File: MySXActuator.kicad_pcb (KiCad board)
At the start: 2 copper layers, 27.7 x 38.1 mm, 30 parts, among them Q1 2N7002, Q2 IRF540N, Q3 IRF540N, Q4 2N7002, U1 AP63205WU

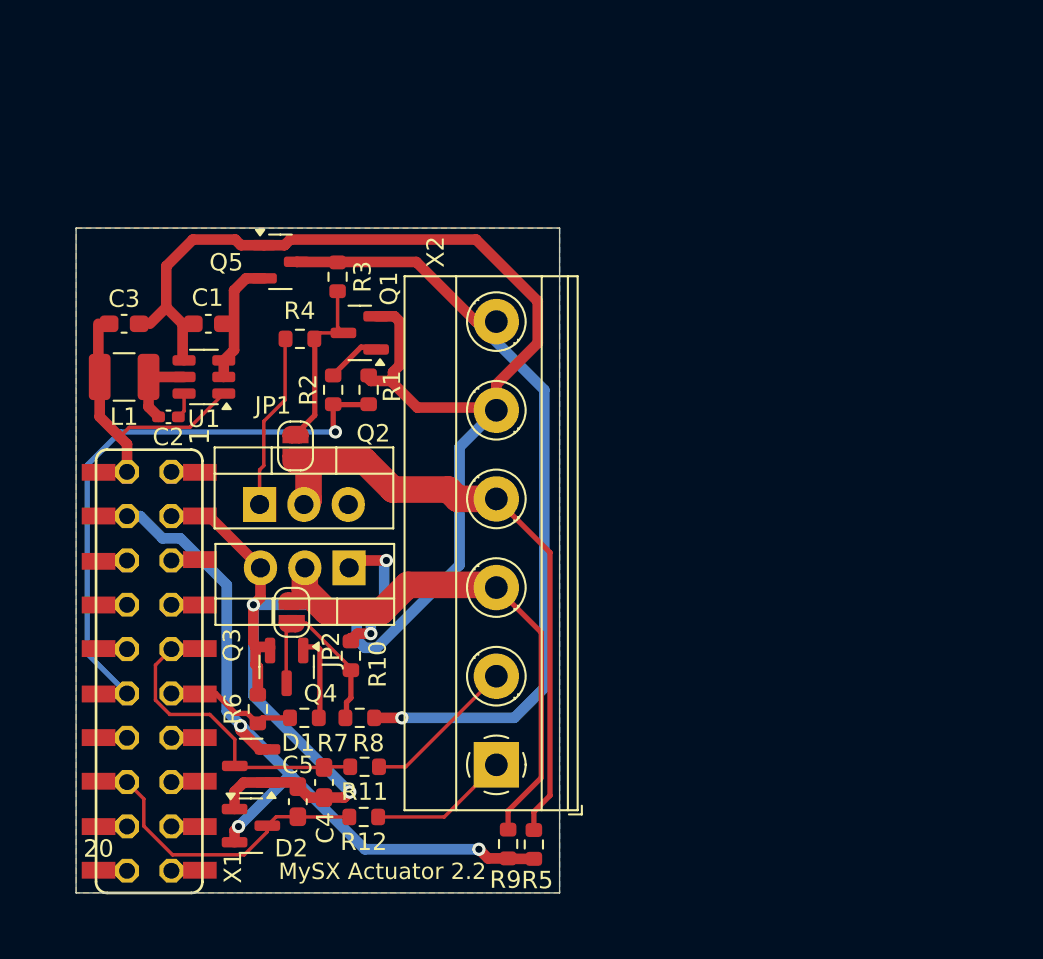
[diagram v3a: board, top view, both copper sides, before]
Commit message: update schematic
- add zener diode to protect high positive voltage on inputs
- add anoter 2 input sections as alternative to led drivers
- add add rj45 socket for i2c interface
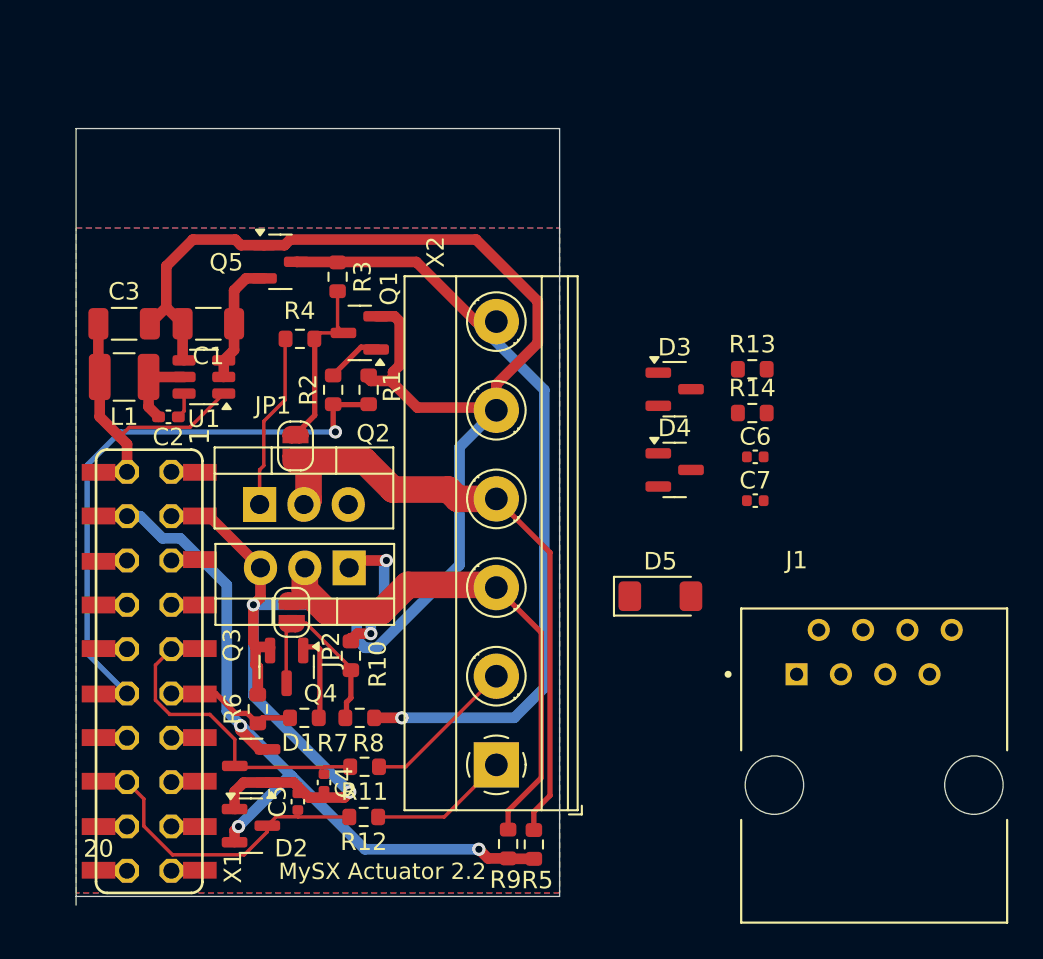
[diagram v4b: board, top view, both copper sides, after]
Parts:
- added C6: 10n/50V, Capacitor_SMD:C_0402_1005Metric, F.Cu at (174.2, 99.1)
- added C7: 10n/50V, Capacitor_SMD:C_0402_1005Metric, F.Cu at (174.2, 101.6)
- added D3: BAT54S, Package_TO_SOT_SMD:SOT-23, F.Cu at (169.6, 95.2)
- added D4: BAT54S, Package_TO_SOT_SMD:SOT-23, F.Cu at (169.6, 99.8)
- added D5: 3.6V, Diode_SMD:D_MiniMELF, F.Cu at (168.8, 107.0)
- added J1: 8P8C, MySXActuator:AMPHENOL_54601-908WPLF, F.Cu at (181.0, 117.9)
- added R13: 2k, Resistor_SMD:R_0603_1608Metric, F.Cu at (174.0, 94.0)
- added R14: 2k, Resistor_SMD:R_0603_1608Metric, F.Cu at (174.0, 96.6)
- C1, C3: footprint Capacitor_SMD:C_0603_1608Metric_Pad1.08x0.95mm_HandSolder -> Capacitor_SMD:C_1206_3216Metric
- C4, C5: value 10n -> 10n/50V; footprint Capacitor_SMD:C_0603_1608Metric_Pad1.08x0.95mm_HandSolder -> Capacitor_SMD:C_0402_1005Metric
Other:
- board size 27.7 x 38.1 mm -> 27.7 x 44.5 mm

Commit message: update PCB after schematic changes
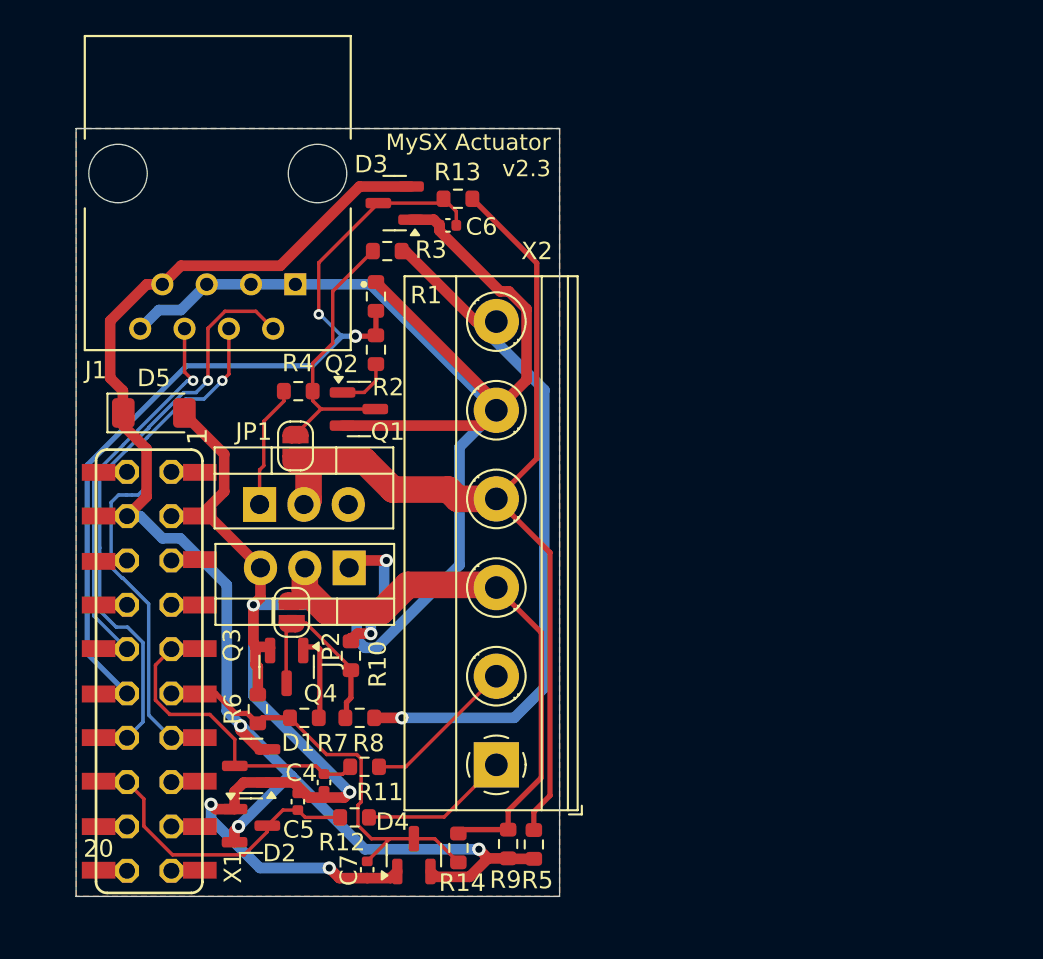
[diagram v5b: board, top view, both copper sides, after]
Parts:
- removed C1: 10u/50V, Capacitor_SMD:C_1206_3216Metric
- removed C2: 100n/50V, Capacitor_SMD:C_0402_1005Metric_Pad0.74x0.62mm_HandSolder
- removed C3: 10u, Capacitor_SMD:C_1206_3216Metric
- removed L1: 4.7u, Inductor_SMD:L_1210_3225Metric
- removed Q5: ~, Package_TO_SOT_SMD:SOT-23
- removed U1: AP63205WU, Package_TO_SOT_SMD:TSOT-23-6
- moved J1 51.4 mm to (143.4, 82.8), turned to 180 degrees
- moved D5 30.9 mm to (139.8, 96.5)
- moved C7 30.7 mm to (152.0, 122.7), turned to -90 degrees
- moved R14 30.1 mm to (157.2, 121.5), turned to -90 degrees
- moved D4 26.7 mm to (154.7, 121.9), turned to 90 degrees
- moved C6 22.0 mm to (156.6, 85.8), turned to 180 degrees
- moved R13 19.5 mm to (157.2, 84.3), turned to 180 degrees
- moved D3 19.3 mm to (153.6, 84.5), turned to 180 degrees
- moved R1 5.37 mm to (152.5, 89.9)
- moved Q1 4.36 mm to (151.5, 96.3), turned to 0 degrees
- moved R2 3.36 mm to (152.5, 92.9), turned to -90 degrees
- moved R3 3.20 mm to (153.1, 87.3), turned to 180 degrees
- moved R4 3.00 mm to (148.0, 95.3)
- moved R12 0.53 mm to (151.2, 119.7)
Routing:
- net VCCIO: track 43.2 -> 80.0 mm
- net D7_SCL: track 0.00 -> 32.8 mm, vias 0 -> 1
- net GND: track 113.2 -> 143.0 mm, vias 2 -> 4
- net D8_SDA: track 0.00 -> 29.0 mm, vias 0 -> 1
- net D3_INT: track 0.00 -> 22.1 mm, vias 0 -> 1
- net LED1: track 35.7 -> 55.4 mm
- net D5_PWM: track 32.7 -> 50.4 mm, vias 1 -> 2
- net D6_PWM: track 7.68 -> 25.1 mm
- net VRAW: track 16.2 -> 0.00 mm
- net Net-(Q5-S): track 7.21 -> 0.00 mm
- net VIN: track 46.1 -> 40.4 mm
- net Net-(JP1-A): track 10.3 -> 15.9 mm
- net Net-(U1-SW): track 4.56 -> 0.00 mm
- net Net-(Q2-G): track 10.1 -> 7.12 mm
- net LED2: track 31.0 -> 33.9 mm
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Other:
- board size 27.7 x 44.5 mm -> 27.7 x 44 mm
- board text added: "MySX Actuator v2.3"
- board text removed: "MySX Actuator 2.2"

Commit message: Add removed buck converter
- previously removed buck converter is needed to not require power from
RS485 line
- position RJ45 connector closer to center of the board to allow use
straigth connector (facing up)
- replace THT power transistors with SMT power transistors
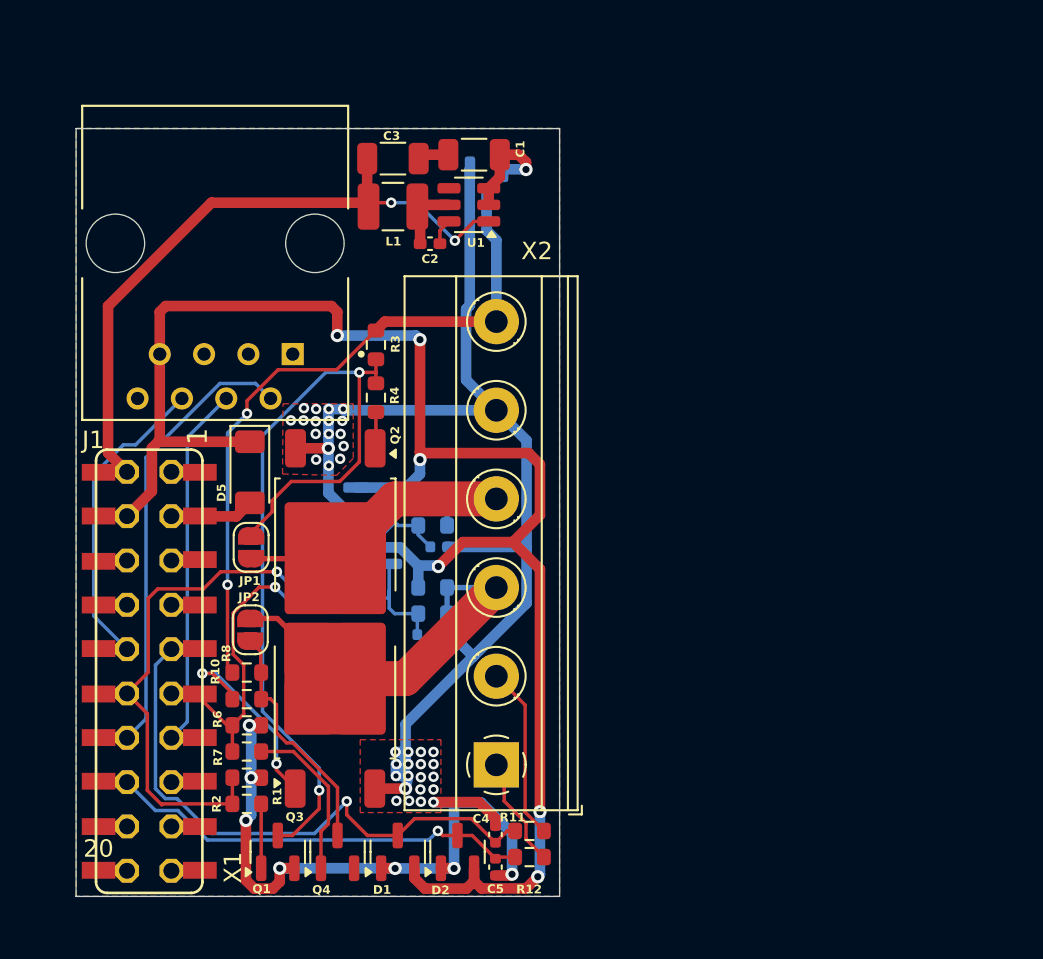
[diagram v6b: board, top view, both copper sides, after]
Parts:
- added C1: 10u/50V, Capacitor_SMD:C_1206_3216Metric, F.Cu at (158.1, 81.8)
- added C2: 100n/50V, Capacitor_SMD:C_0402_1005Metric_Pad0.74x0.62mm_HandSolder, F.Cu at (155.6, 86.8)
- added C3: 10u, Capacitor_SMD:C_1206_3216Metric, F.Cu at (153.4, 82.0)
- added L1: 4.7u, Inductor_SMD:L_1210_3225Metric, F.Cu at (153.4, 84.7)
- added Q5: ~, Package_TO_SOT_SMD:SOT-23, B.Cu at (158.8, 83.5)
- added U1: AP63205WU, Package_TO_SOT_SMD:TSOT-23-6, F.Cu at (157.8, 84.6)
- C6, C7, D3, D4, R13, R14, R5, R9: moved to B.Cu
- Q2, Q3: value IRF540N -> IRFR7546PbF; footprint Package_TO_SOT_THT:TO-220-3_Vertical -> Package_TO_SOT_SMD:TO-252-2
- moved R1 28.6 mm to (145.1, 117.5), turned to 0 degrees
- moved R2 27.1 mm to (145.1, 119.0), turned to 0 degrees
- moved Q1 25.8 mm to (146.8, 121.7), turned to 90 degrees
- moved R5 20.6 mm to (155.7, 101.5), turned to 0 degrees
- moved R13 18.8 mm to (155.7, 103.0)
- moved C6 18.4 mm to (156.1, 104.2), turned to 0 degrees
- moved D3 17.3 mm to (152.3, 101.8), turned to 0 degrees
- moved D4 16.9 mm to (152.3, 105.2), turned to 0 degrees
- moved R9 15.3 mm to (155.7, 106.5), turned to 0 degrees
- moved C7 13.9 mm to (155.3, 109.2), turned to 0 degrees
- moved R14 13.5 mm to (155.7, 108.0), turned to 180 degrees
- moved D2 11.9 mm to (157.2, 121.7), turned to 90 degrees
- moved C5 11.9 mm to (159.3, 122.6), turned to -90 degrees
- moved Q4 11.0 mm to (150.3, 121.7), turned to 90 degrees
- moved R12 10.3 mm to (161.3, 122.0)
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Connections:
- net D3_RX renamed D2_RX
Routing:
- net VRAW: track 0.00 -> 38.3 mm, vias 0 -> 2
- net LED1: track 55.4 -> 19.8 mm
- net Net-(JP1-A): track 15.9 -> 48.7 mm, vias 0 -> 2
- net VCCIO: track 80.0 -> 99.7 mm, vias 3 -> 6
- net GND: track 143.0 -> 126.0 mm, vias 4 -> 43
- net D4_INT: track 17.3 -> 33.3 mm, vias 0 -> 1
- net LED2: track 33.9 -> 19.8 mm
- net D8_SDA: track 29.0 -> 20.7 mm, vias 1 -> 0
- net D9_A3: track 16.3 -> 24.5 mm, vias 0 -> 1
- net D7_SCL: track 32.8 -> 25.8 mm, vias 1 -> 0
- net +24V: track 0.00 -> 6.56 mm, vias 0 -> 1
- net Net-(Q2-G): track 7.12 -> 2.09 mm
- net D5_PWM: track 50.4 -> 45.4 mm, vias 2 -> 1
- net Net-(Q4-G): track 4.97 -> 9.54 mm
- net D3_INT: track 22.1 -> 17.7 mm, vias 1 -> 0
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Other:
- board text added: "GND"
- board text added: "LED1"
- board text added: "LED2"
- board text added: "MySX Actuator v2.4"
- board text added: "SW1"
- board text added: "SW2"
- board text added: "VIN"
- board text removed: "MySX Actuator v2.3"

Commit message: update to new kicad version 8.0
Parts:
- Q5: value ~ -> BSS84A
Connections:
- net D10_A4 renamed D10_A4_1
- net D11_MOSI renamed D11_MOSI_1
- net D12_MISO renamed D12_MISO_1
- net D13_SCK renamed D13_SCK_1
- net D14_CS renamed D14_CS_1
- net D1_TX renamed D1_TX_1
- net D2_RX renamed D2_RX_1
- net LEGACY_ID renamed LEGACY_ID_1
- net RST renamed RST_1

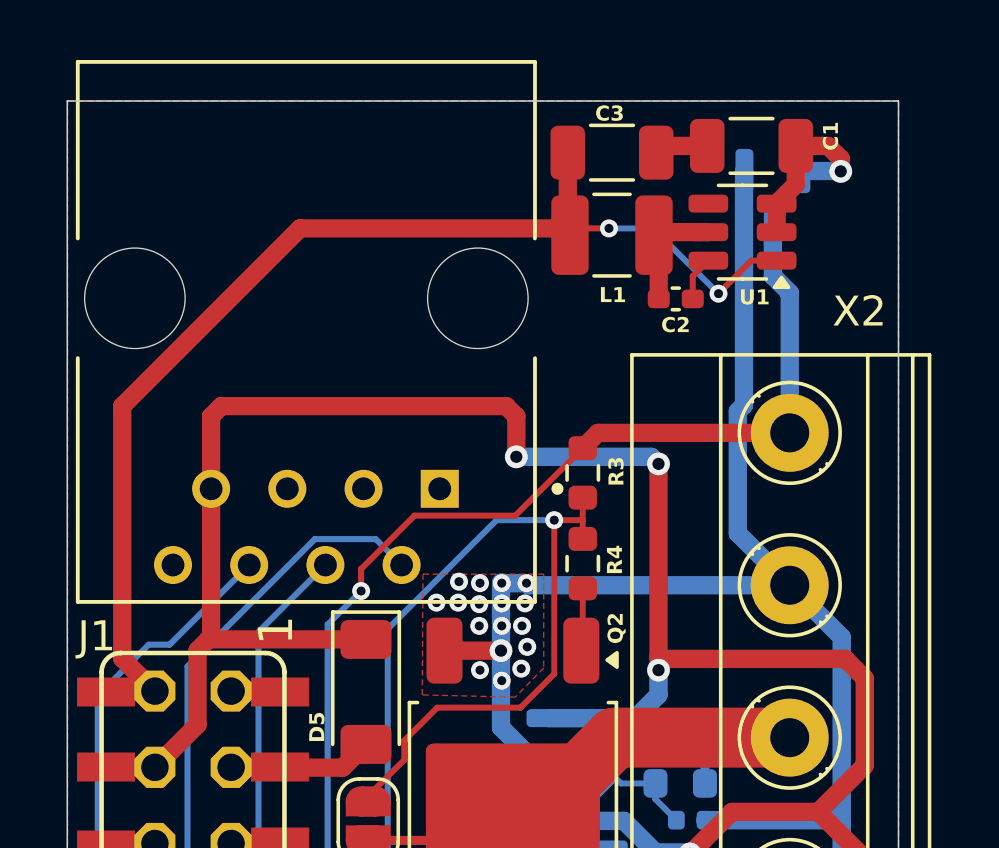
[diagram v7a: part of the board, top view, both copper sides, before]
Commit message: add input voltage transient protection
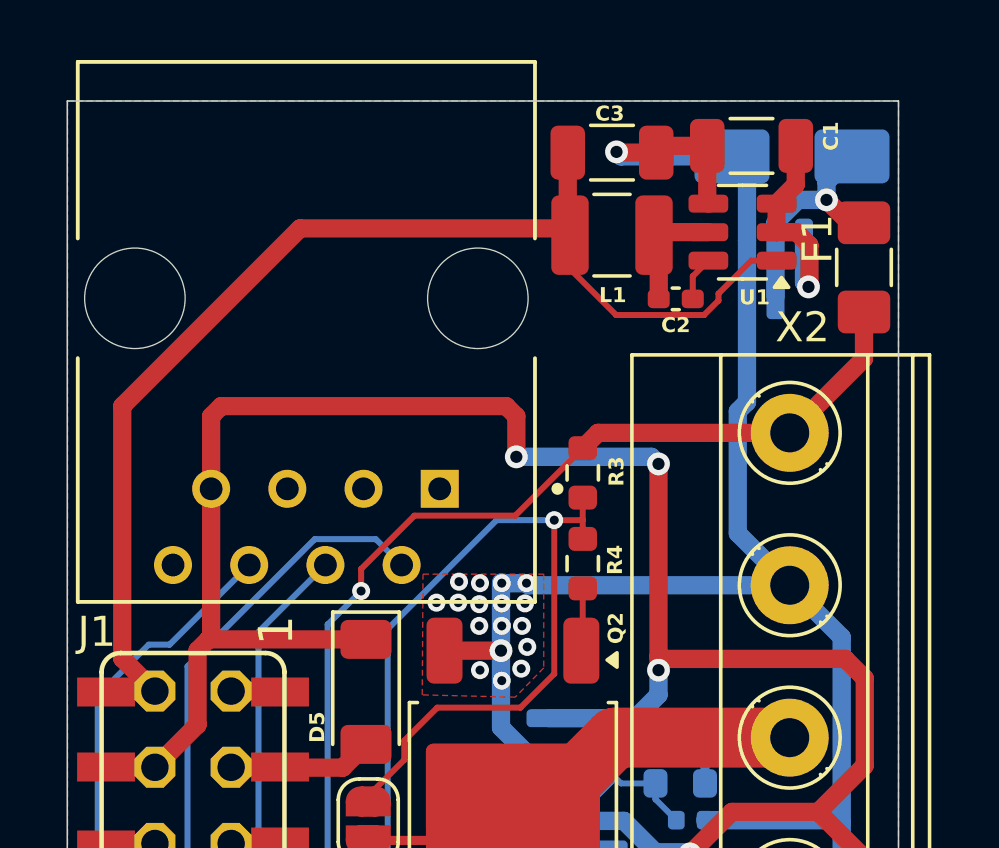
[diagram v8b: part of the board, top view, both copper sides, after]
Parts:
- added D6: SMAJ26CA, Diode_SMD:D_SMA, B.Cu at (159.4, 82.1)
- added F1: PTS120660V010, Fuse:Fuse_1206_3216Metric_Pad1.42x1.75mm_HandSolder, F.Cu at (161.8, 85.8)
- moved Q5 2.33 mm to (158.9, 85.8)
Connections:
- net D10_A4_1 renamed D10_A4
- net D11_MOSI_1 renamed D11_MOSI
- net D12_MISO_1 renamed D12_MISO
- net D13_SCK_1 renamed D13_SCK
- net D14_CS_1 renamed D14_CS
- net D1_TX_1 renamed D1_TX
- net D2_RX_1 renamed D2_RX
- net LEGACY_ID_1 renamed LEGACY_ID
- net RST_1 renamed RST
- Q5 pad 3: VIN -> Net-(D6-A2)
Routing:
- net GND: track 126.0 -> 133.9 mm, vias 43 -> 44
- net Net-(D6-A2): track 0.00 -> 7.87 mm, vias 0 -> 1
- net VIN: track 39.5 -> 37.5 mm
- net VRAW: track 38.3 -> 39.6 mm, vias 2 -> 0
- net +24V: track 6.56 -> 7.42 mm
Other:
- board text added: "MySX Actuator v2.5"
- board text removed: "MySX Actuator v2.4"
